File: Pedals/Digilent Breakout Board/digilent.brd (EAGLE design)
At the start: 66 x 57.1 mm, 5 parts

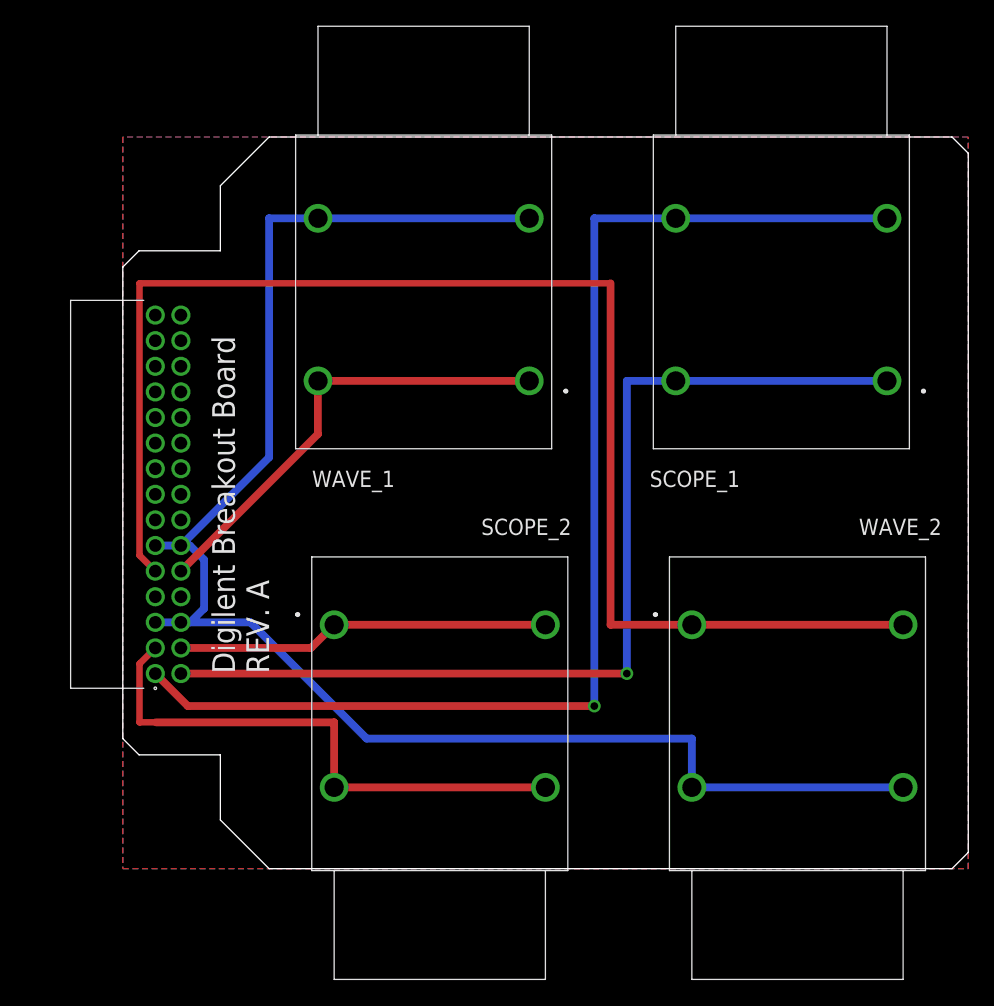
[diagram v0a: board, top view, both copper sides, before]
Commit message: Put correct header on the digilent PCB
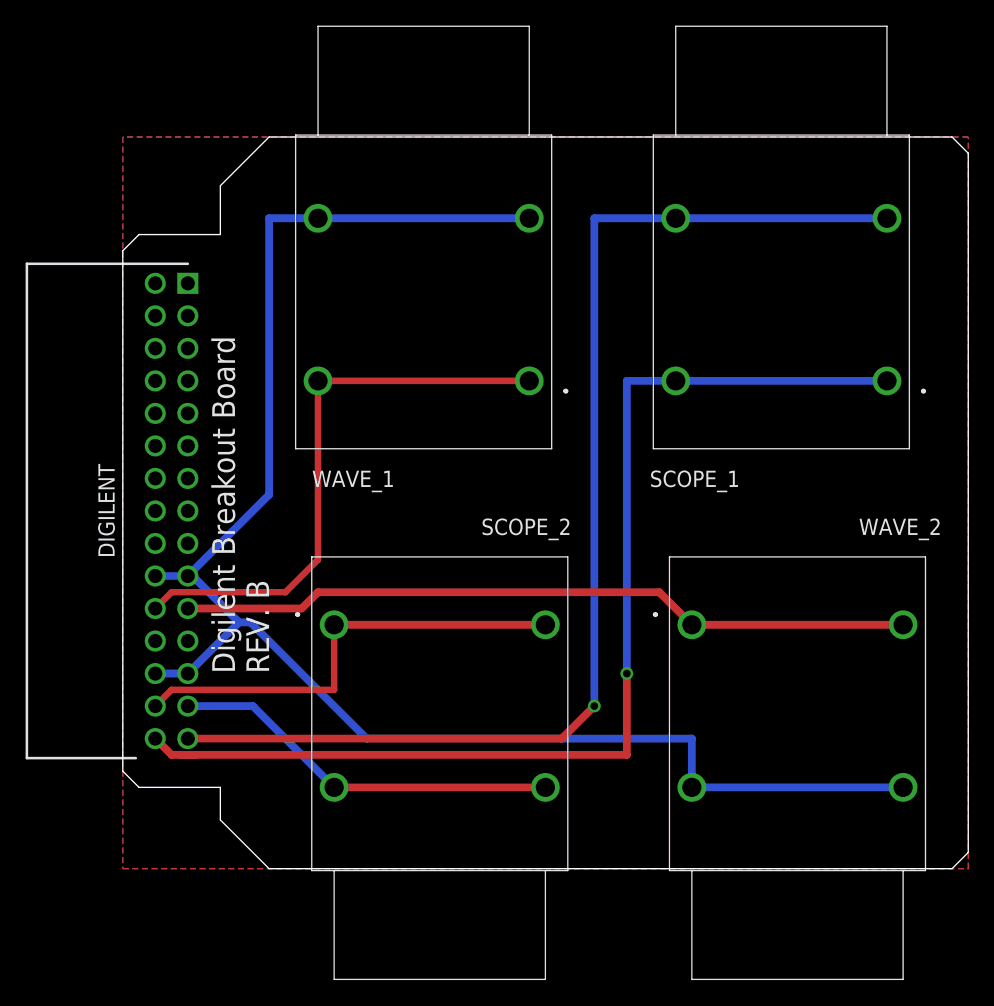
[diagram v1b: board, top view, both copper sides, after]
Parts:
- DIGILENT: value SQT-115-01-F-D-RA -> SSQ-115-02-T-D-RA; device SamacSys_Parts:SQT-115-01-XXX-D-RA -> SamacSys_Parts:RHDRRA30W64P254_2X15_3861X851X
- moved DIGILENT 30.6 mm to (5.08, 45.7), turned to 90 degrees
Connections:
- net AGND: now also DIGILENT.19, DIGILENT.20, DIGILENT.25, DIGILENT.26; no longer DIGILENT.11, DIGILENT.12, DIGILENT.5, DIGILENT.6
- net SC1_N: now also DIGILENT.29; no longer DIGILENT.1
- net SC1_P: now also DIGILENT.30; no longer DIGILENT.2
- net SC2_N: now also DIGILENT.27; no longer DIGILENT.3
- net SC2_P: now also DIGILENT.28; no longer DIGILENT.4
- net WV_1: now also DIGILENT.22; no longer DIGILENT.10
- net WV_2: now also DIGILENT.21; no longer DIGILENT.9
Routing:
- net WV_2: track 109.3 -> 57.4 mm
- net SC2_N: track 43.1 -> 30.6 mm
- net WV_1: track 35.8 -> 44.8 mm
- net SC1_P: track 78.0 -> 86.9 mm
- net SC2_P: track 29.2 -> 36.1 mm
- net SC1_N: track 96.3 -> 93.8 mm
- net AGND: track 125.1 -> 126.6 mm
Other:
- outline, holes or cut-outs redrawn
- board text added: "Digilent Breakout Board REV. B"
- board text removed: "Digilent Breakout Board REV. A"
